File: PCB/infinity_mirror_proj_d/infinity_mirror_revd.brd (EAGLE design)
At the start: 64 x 29 mm, 35 parts, among them J1 5.5x2.1mm Barrel, J2 HEADER, Q1 800mA/40V, Q2 800mA/40V, Q3 BSS138, U1 3.3LDO

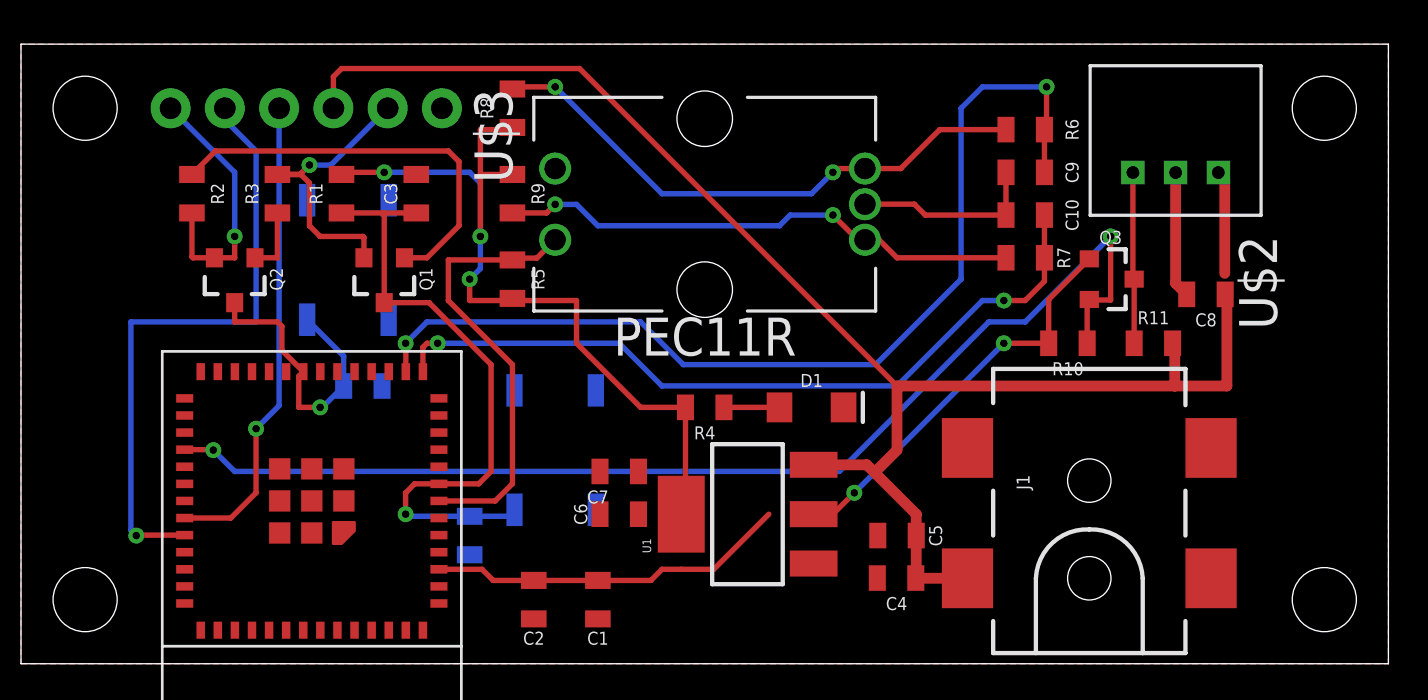
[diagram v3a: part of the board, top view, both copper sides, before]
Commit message: fixed airwires and changed programming header from 6 pins to 4 pins
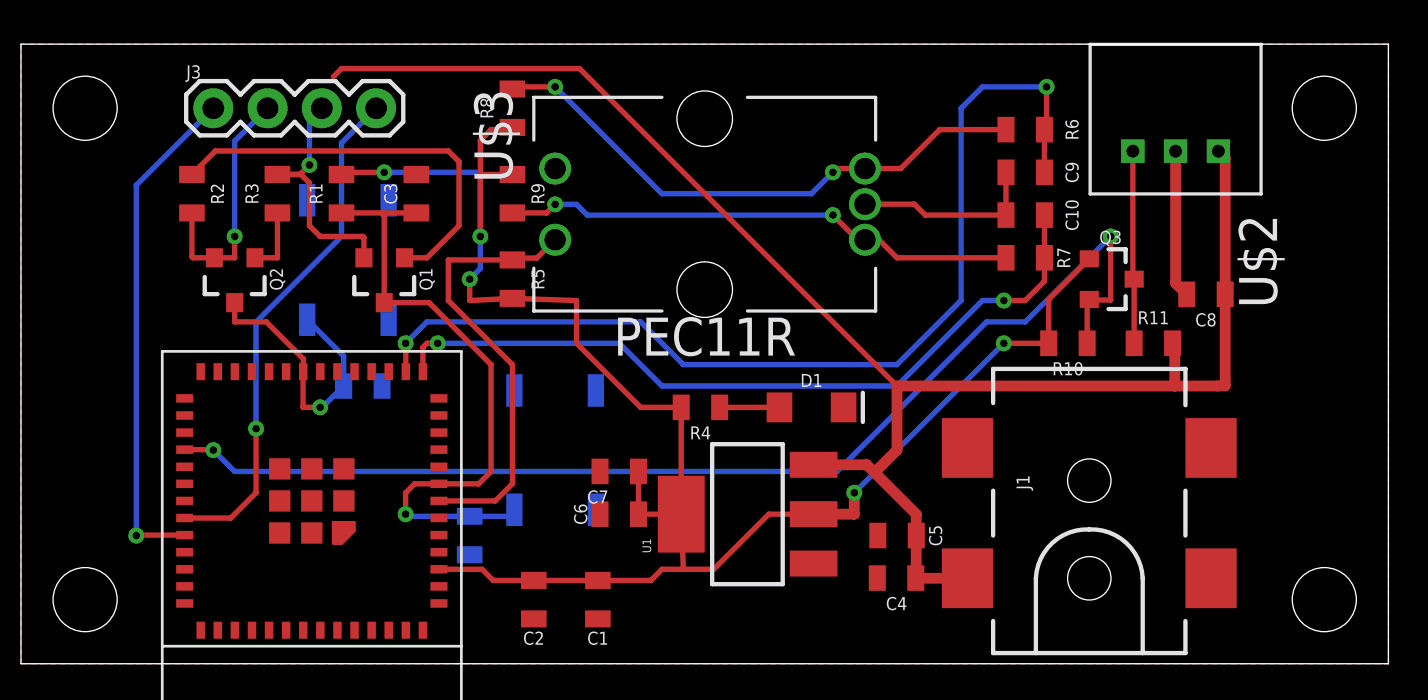
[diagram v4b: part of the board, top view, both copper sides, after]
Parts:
- removed J2: HEADER, SparkFun-Connectors:1X06
- added J3: (no value), SparkFun-Connectors:1X04
- moved U$2 1.00 mm to (54.0, 24.0)
- moved R4 0.20 mm to (31.8, 12.0)
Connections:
- net DTR: now also J3.2; no longer J2.1
- net GND: no longer J2.6
- net RTS: now also J3.3; no longer J2.5
- net U0RXD: now also J3.4; no longer J2.3
- net U0TXD: now also J3.1; no longer J2.2
- net VCC_1: no longer J2.4
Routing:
- net VCC_2: track 74.1 -> 84.2 mm
- net U0TXD: track 28.8 -> 23.8 mm
- net U0RXD: track 22.3 -> 24.2 mm
- net RTS: track 13.8 -> 12.0 mm
- net LED_DATA: track 8.01 -> 9.01 mm
- net GND: track 14.7 -> 15.7 mm
- net DTR: track 12.3 -> 11.7 mm
- net GPIO0: track 13.8 -> 13.2 mm
- net ENC_B: track 46.7 -> 47.3 mm
- net VCC_1: track 76.4 -> 76.9 mm

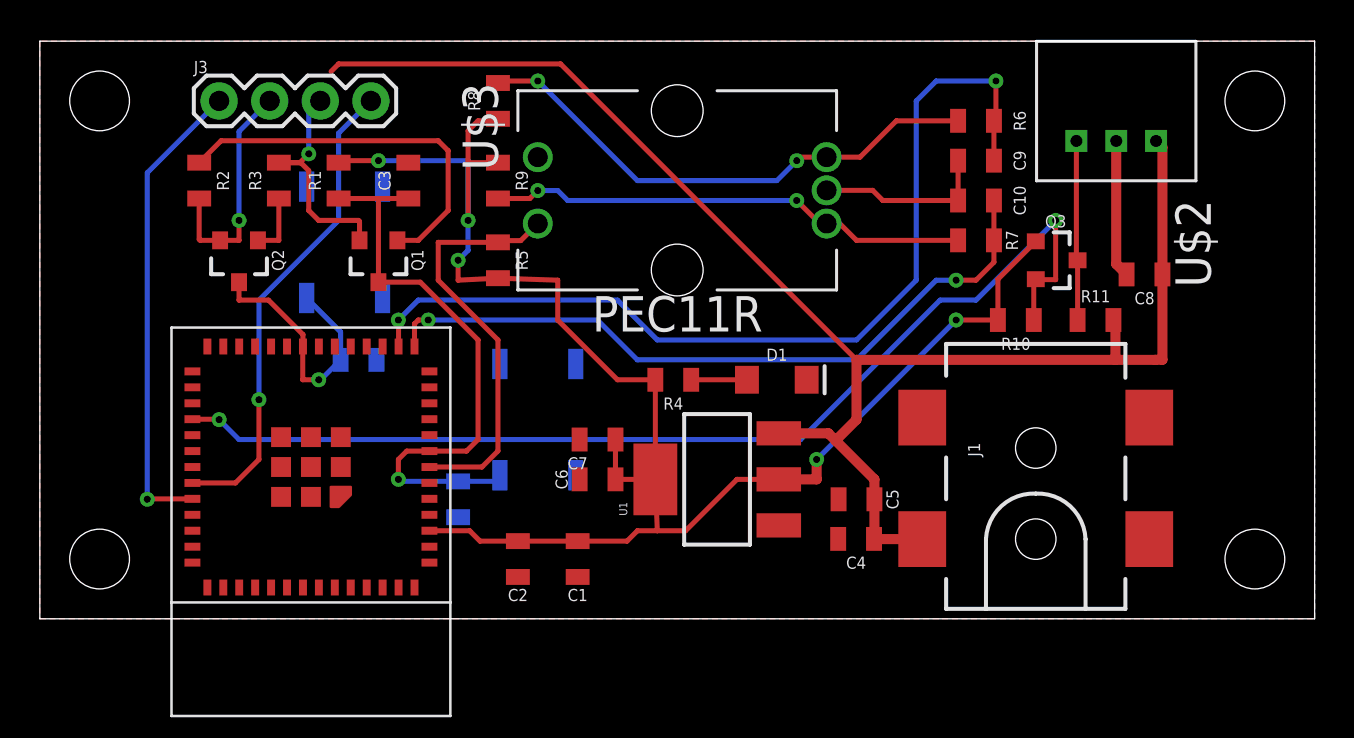
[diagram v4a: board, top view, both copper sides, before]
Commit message: more airwires. cleaned up silk. changed LED cap to leaded electrolytic
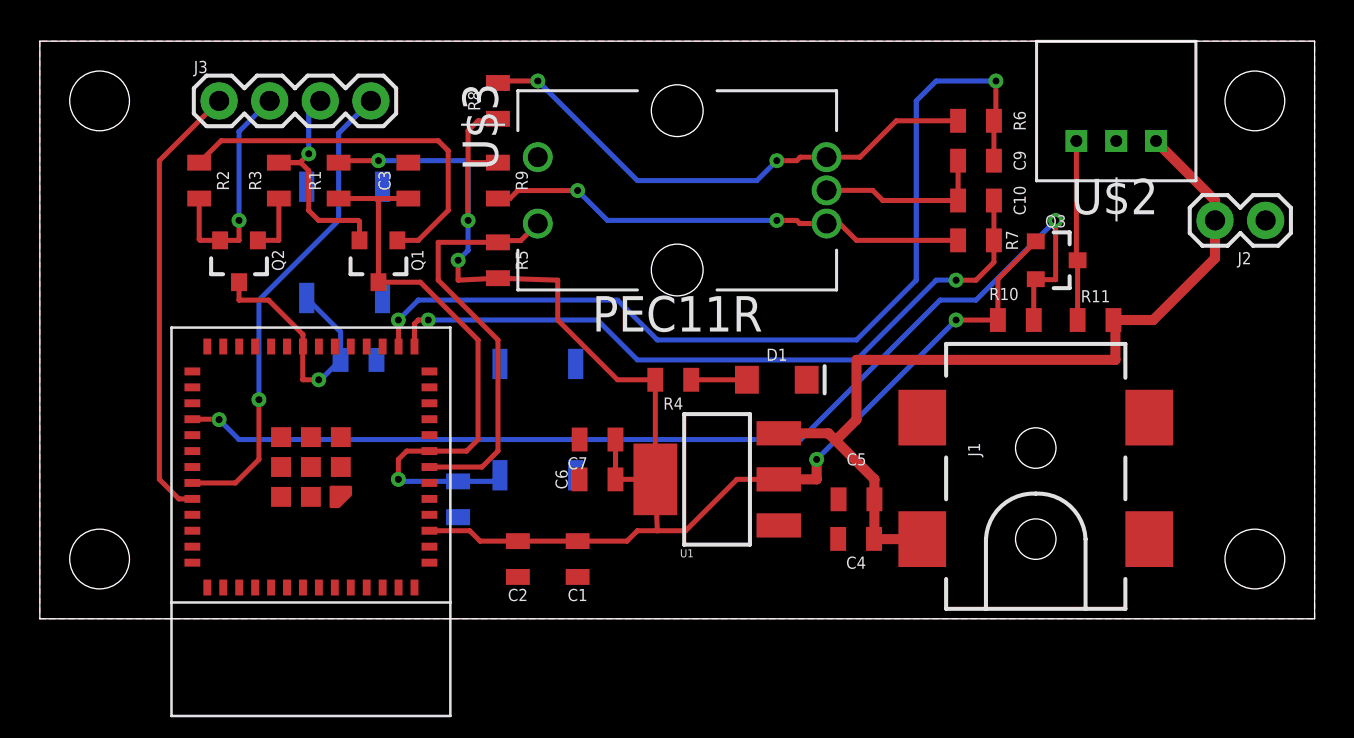
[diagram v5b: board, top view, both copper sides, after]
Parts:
- removed C8: 1000uF, _111_IH:0805
- added J2: (no value), SparkFun-Connectors:1X02
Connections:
- new net N$1: J2.2
- net GND: no longer C8.2
- net VCC_1: now also J2.1; no longer C8.1
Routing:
- net VCC_1: track 76.9 -> 44.2 mm
- net GND: track 15.7 -> 8.81 mm
- net U0TXD: track 23.8 -> 22.3 mm, vias 1 -> 0
- added copper zone on layer 16, net GND

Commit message: not sure
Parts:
- J1: value 5.5x2.1mm Barrel -> POWER_JACKPTH_BREAD; device SparkFun-Connectors:POWER_JACK_SMD -> SparkFun-Connectors:POWER_JACK_PTH_BREAD
- moved J1 7.28 mm to (48.0, -3.00), turned to 0 degrees
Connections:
- net GND: now also J1.GNDBREAK; no longer J1.P$4
- net VCC_1: now also J1.PWR; no longer J1.VIN0
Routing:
- net VCC_1: track 44.2 -> 52.3 mm
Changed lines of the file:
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@@
 <attribute name="VALUE" x="8.349" y="18" size="0.6096" layer="27" font="vector" ratio="20" rot="R270" align="top-center"/>
 </element>
-<element name="J1" library="SparkFun-Connectors" package="POWER_JACK_SMD" value="5.5x2.1mm Barrel" x="50" y="4" smashed="yes" rot="R90">
-<attribute name="NAME" x="47.206" y="8.1402" size="0.6096" layer="25" font="vector" ratio="20" rot="R90"/>
-<attribute name="PROD_ID" value="CONN-08106" x="50" y="4" size="1.778" layer="27" rot="R90" display="off"/>
-<attribute name="SF_ID" value="PRT-12748" x="50" y="4" size="1.778" layer="27" rot="R90" display="off"/>
-<attribute name="VALUE" x="58.002" y="3.01" size="0.6096" layer="27" font="vector" ratio="20" rot="R90"/>
+<element name="J1" library="SparkFun-Connectors" library_urn="urn:adsk.eagle:library:513" package="POWER_JACK_PTH_BREAD" package3d_urn="urn:adsk.eagle:package:38228/1" value="POWER_JACKPTH_BREAD" x="48" y="-3" smashed="yes">
+<attribute name="NAME" x="52.1402" y="-0.206" size="0.6096" layer="25" font="vector" ratio="20"/>
+<attribute name="PROD_ID" value="PRT-10811" x="48" y="-3" size="1.778" layer="27" display="off"/>
 </element>
 <element name="U1" library="SparkFun-IC-Power" library_urn="urn:adsk.eagle:library:526" package="SOT223" package3d_urn="urn:adsk.eagle:package:39069/1" value="3.3LDO" x="34" y="7" smashed="yes" rot="R90">
@@
 <contactref element="C2" pad="2"/>
 <contactref element="U$1" pad="27"/>
+<contactref element="J1" pad="GNDBREAK"/>
 <contactref element="J1" pad="GND"/>
-<contactref element="J1" pad="P$4"/>
 <contactref element="U1" pad="1"/>
 <contactref element="C5" pad="2"/>
@@
 <contactref element="U1" pad="3"/>
 <contactref element="C4" pad="1"/>
-<contactref element="J1" pad="VIN0"/>
+<contactref element="J1" pad="PWR"/>
 <contactref element="C5" pad="1"/>
-<wire x1="44.3" y1="4" x2="41.89" y2="4" width="0.508" layer="1"/>
 <wire x1="41.89" y1="4" x2="41.88" y2="4.01" width="0.508" layer="1"/>
 <wire x1="41.9" y1="6" x2="41.9" y2="4.03" width="0.508" layer="1"/>
@@
 <wire x1="56.04" y1="23.96" x2="56.04" y2="23.99" width="0.508" layer="1"/>
 <wire x1="59" y1="21" x2="56.04" y2="23.96" width="0.508" layer="1"/>
+<wire x1="41.89" y1="4" x2="44" y2="4" width="0.508" layer="1"/>
+<wire x1="44" y1="4" x2="44" y2="5.7" width="0.508" layer="1"/>
+<wire x1="48" y1="9.7" x2="48" y2="10.7" width="0.508" layer="1"/>
+<wire x1="48" y1="9.7" x2="44" y2="5.7" width="0.508" layer="1"/>
 </signal>
 <signal name="LED+">

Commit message: pcb refactor
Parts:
- J2: value (none) -> CAP
- J3: value (none) -> SERIAL
- moved C9 26.4 mm to (23.0, 34.0), turned to 270 degrees
- moved R6 23.8 mm to (25.0, 34.0), turned to 270 degrees
- moved C10 21.0 mm to (28.0, 30.0)
- moved R7 21.0 mm to (28.0, 28.0)
- moved R5 16.5 mm to (37.0, 26.7)
- moved J1 16.0 mm to (32.0, -3.00)
- moved R2 15.0 mm to (20.0, 31.0), turned to 180 degrees
- moved U$2 12.1 mm to (46.0, 15.0), turned to 0 degrees
- moved Q2 11.7 mm to (16.0, 28.0)
- moved C11 11.6 mm to (14.5, 24.5), flipped to the top, turned to 270 degrees
- moved R11 11.3 mm to (45.0, 23.0), turned to 180 degrees
- moved U1 11.2 mm to (32.0, 18.0), turned to 0 degrees
- moved C4 10.5 mm to (37.8, 14.0), turned to 270 degrees
- moved Q1 10.4 mm to (20.0, 28.0)
- moved J2 10.0 mm to (53.0, 12.0)
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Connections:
- removed net N$1: J2.2
- net DTR: now also J3.4; no longer J3.2
- net GND: now also J2.2
- net U0RXD: now also J3.2; no longer J3.4
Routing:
- net ENC_B: track 47.3 -> 19.5 mm
- net N$2: track 26.5 -> 4.38 mm, vias 2 -> 0
- net N$3: track 24.3 -> 5.26 mm, vias 2 -> 0
- net Q1_BASE: track 19.3 -> 2.00 mm
- net ENC_A: track 36.3 -> 21.3 mm
- net ESP_RST: track 29.7 -> 17.3 mm, vias 1 -> 0
- net BUTTON: track 20.9 -> 31.3 mm, vias 0 -> 2
- net GND: track 8.81 -> 0.00 mm
- net VCC_2: track 84.0 -> 91.9 mm, vias 5 -> 0
- net VCC_1: track 52.3 -> 60.1 mm, vias 0 -> 2
- net GPIO0: track 13.2 -> 8.74 mm, vias 1 -> 0
- net LED_DATA: track 9.01 -> 13.5 mm
- net DTR: track 11.7 -> 14.6 mm, vias 1 -> 0
- net IO23: track 54.4 -> 52.8 mm
- net U0TXD: track 22.3 -> 23.6 mm
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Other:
- board size 64 x 29 mm -> 64 x 37 mm
